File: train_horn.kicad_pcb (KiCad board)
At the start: 2 copper layers, 25.4 x 90 mm, 72 parts, among them J1 USB_OTG, J2 PROG, Q1 2N7002, SW1 PLAY, U1 MIC7221, U2 MCP73831, U3 TPS78233DDCR, U4 MSP430FR2000_TSSOP, U5 TPA6211A1

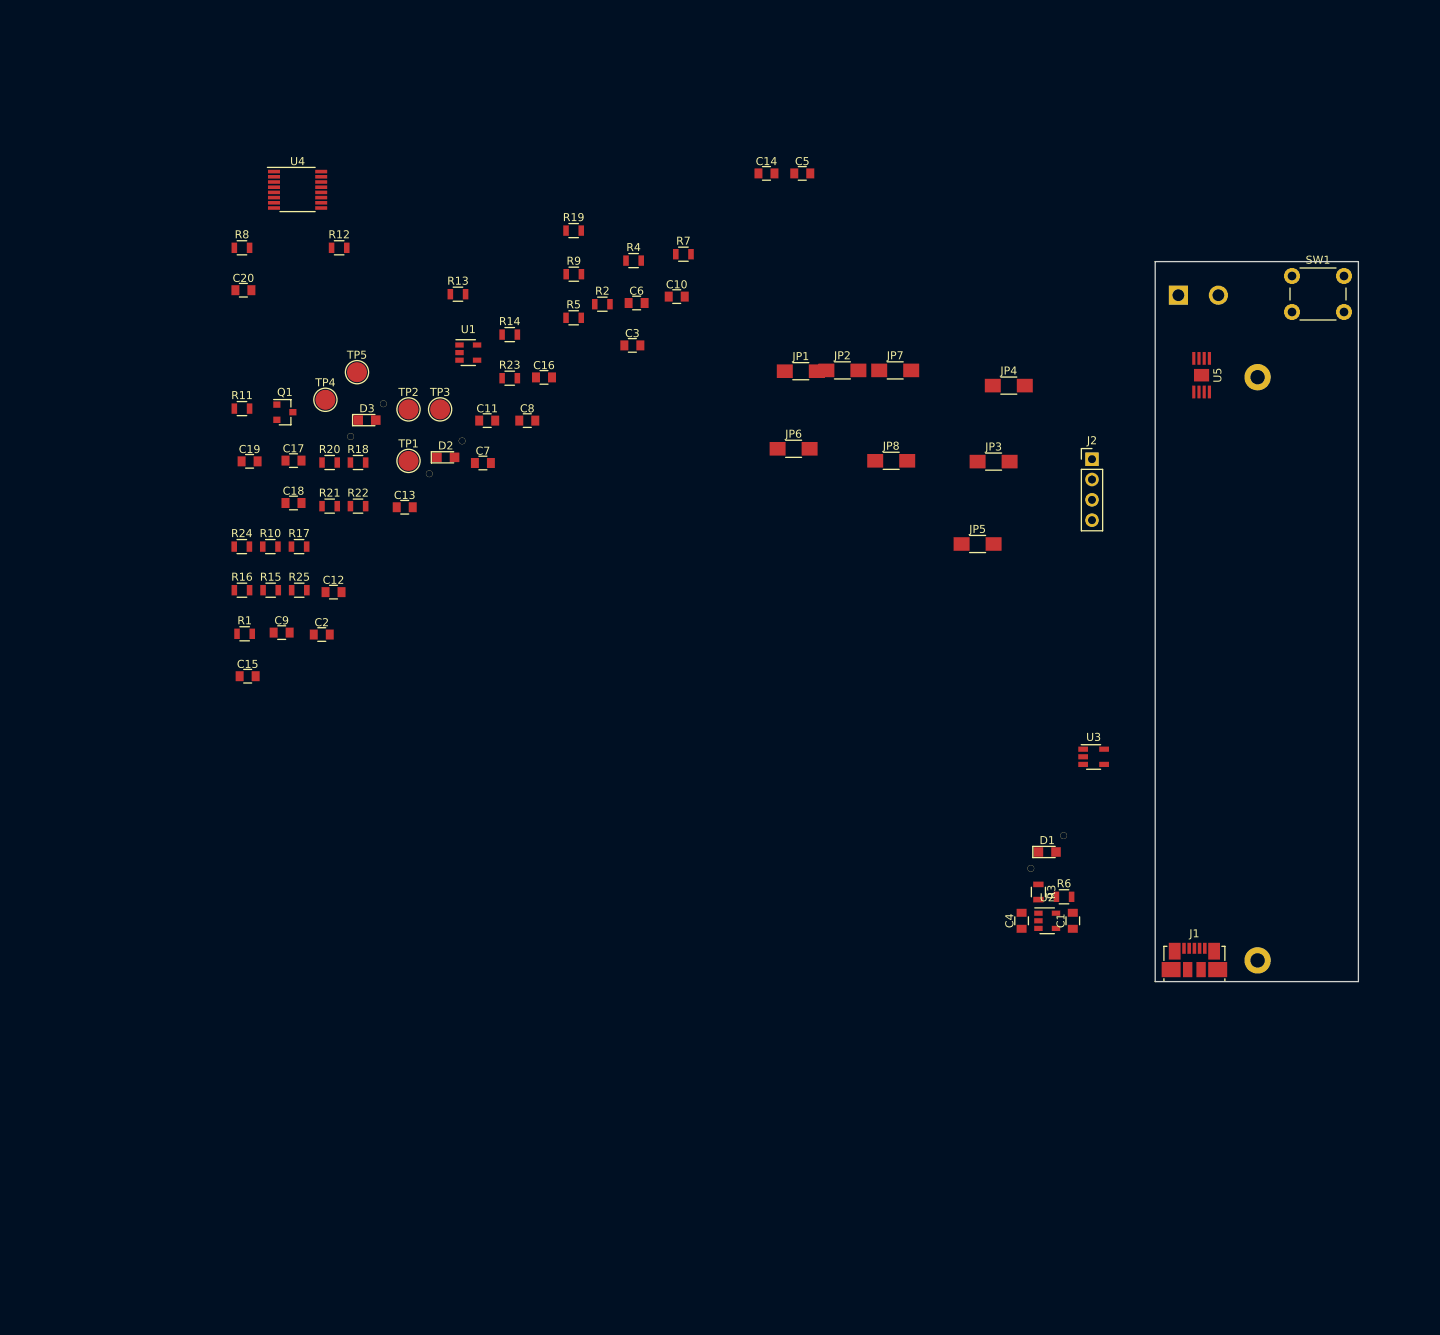
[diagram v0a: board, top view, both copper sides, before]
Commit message: setting large componet location. Change PCB size
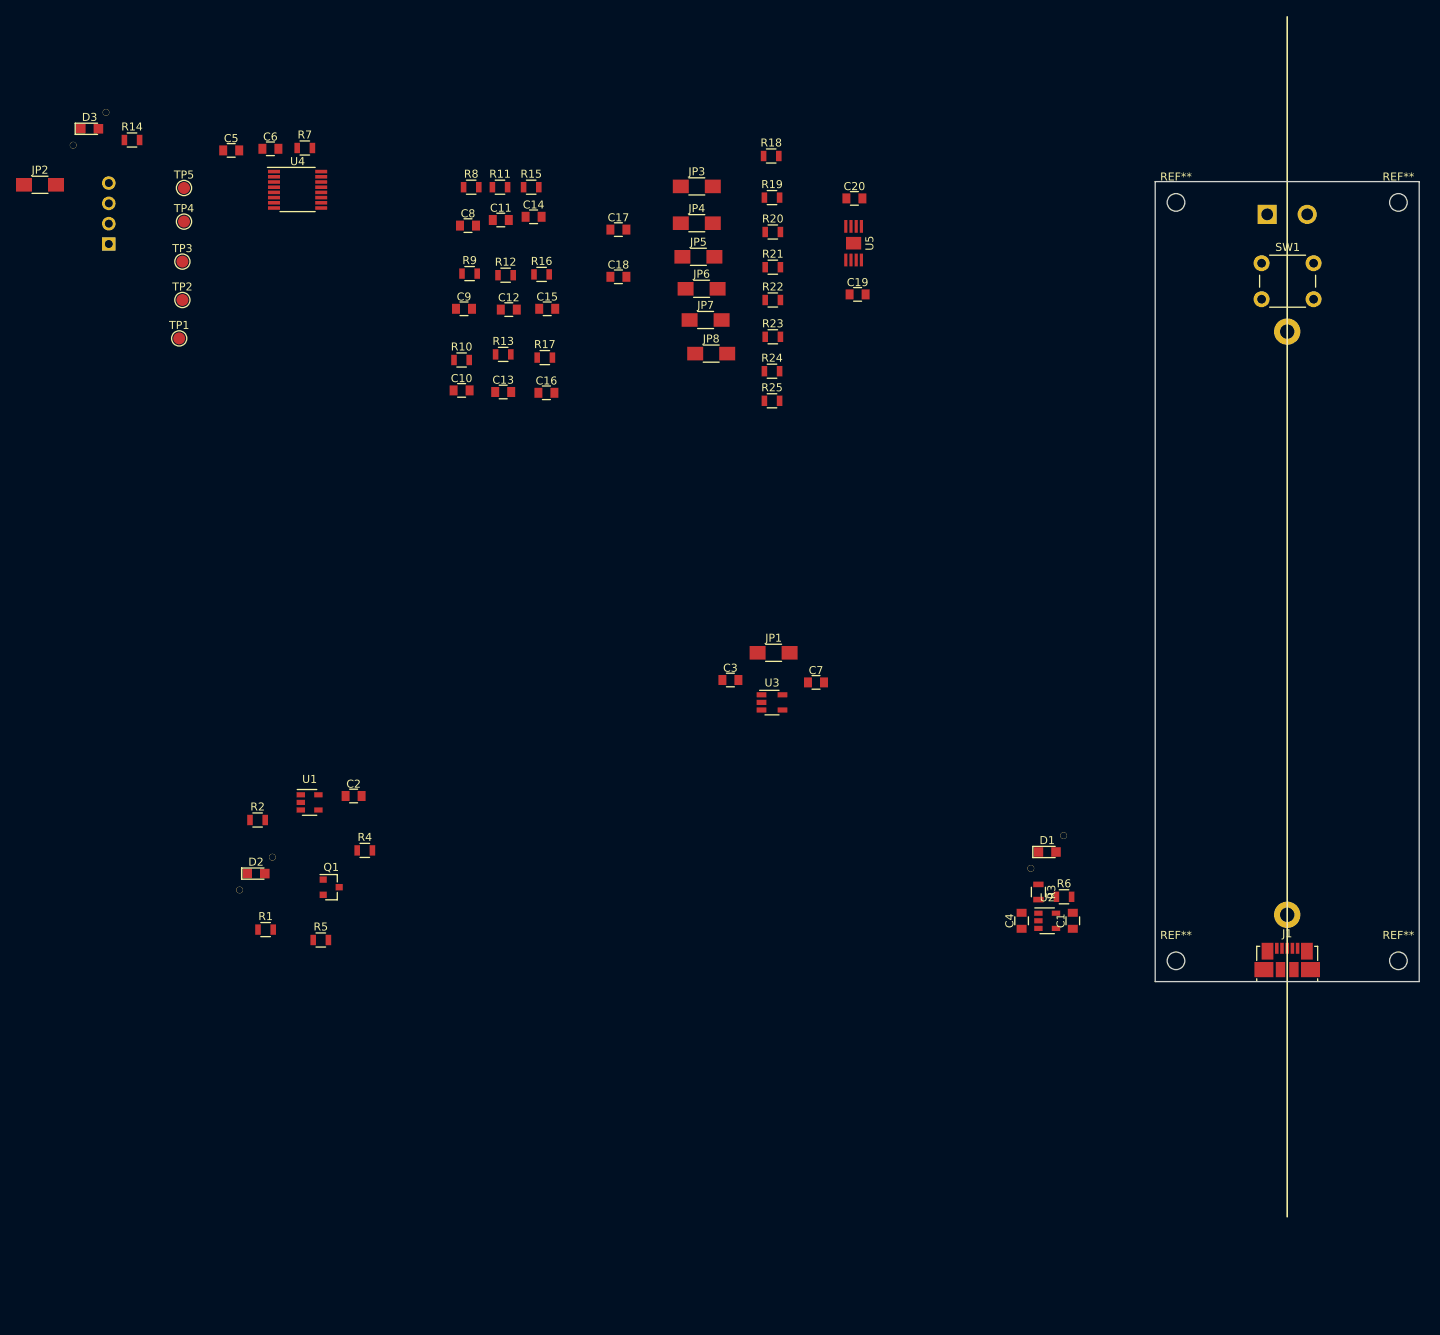
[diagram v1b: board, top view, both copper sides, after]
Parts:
- added REF**: MountingHole_2.2mm_M2, Mounting_Holes:MountingHole_2.2mm_M2, F.Cu at (241.6, 158.0)
- added REF**: MountingHole_2.2mm_M2, Mounting_Holes:MountingHole_2.2mm_M2, F.Cu at (213.8, 158.0)
- added REF**: MountingHole_2.2mm_M2, Mounting_Holes:MountingHole_2.2mm_M2, F.Cu at (213.8, 63.2)
- added REF**: MountingHole_2.2mm_M2, Mounting_Holes:MountingHole_2.2mm_M2, F.Cu at (241.6, 63.2)
- J2: moved to B.Cu
- TP1, TP2, TP3, TP4, TP5: footprint Connectors_TestPoints:Test_Point_Pad_d2.5mm -> Connectors_TestPoints:Test_Point_Pad_d1.5mm
- moved J2 125.8 mm to (80.4, 68.4)
- moved JP2 102.9 mm to (71.8, 61.0)
- moved R5 84.0 mm to (106.9, 155.4)
- moved R4 81.0 mm to (112.4, 144.2)
- moved C19 78.8 mm to (174.0, 74.7)
- moved R2 77.6 mm to (99.0, 140.4)
- moved C20 77.2 mm to (173.6, 62.7)
- moved C5 71.4 mm to (95.7, 56.7)
- moved R24 69.8 mm to (163.3, 84.3)
- moved R18 64.3 mm to (163.2, 57.4)
- moved R25 63.7 mm to (163.3, 88.0)
- moved R21 62.9 mm to (163.4, 71.3)
- moved R20 62.4 mm to (163.4, 66.9)
- moved R15 60.0 mm to (133.2, 61.3)
- moved Q1 59.7 mm to (108.2, 148.8)
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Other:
- board size 25.4 x 90 mm -> 33 x 100 mm

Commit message: moving things around
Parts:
- moved TP5 167.5 mm to (241.7, 132.1)
- moved TP4 164.8 mm to (241.7, 129.5)
- moved TP3 162.2 mm to (241.7, 126.9)
- moved TP2 159.8 mm to (241.7, 124.3)
- moved D3 159.3 mm to (214.3, 136.4), turned to 180 degrees
- moved TP1 158.0 mm to (241.7, 121.7)
- moved JP2 157.4 mm to (217.4, 120.9), turned to 90 degrees
- moved R14 152.2 mm to (221.4, 119.4)
- moved C5 143.7 mm to (222.4, 124.5), turned to 270 degrees
- moved J2 143.0 mm to (214.0, 119.5), turned to 180 degrees
- moved U4 138.2 mm to (227.7, 123.3)
- moved C6 137.8 mm to (220.4, 124.5), turned to 270 degrees
- moved R7 133.4 mm to (221.4, 121.4)
- moved R2 128.8 mm to (227.7, 145.4)
- moved R1 124.9 mm to (224.5, 143.9), turned to 270 degrees
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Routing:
- added copper zone on B.Cu, net GND

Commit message: laying things out
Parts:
- added REF**: VIA_06mm, lib_fp:VIA_0-4mm, F.Cu at (232.7, 71.7)
- added REF**: VIA_06mm, lib_fp:VIA_0-6mm, F.Cu at (236.4, 144.8)
- added REF**: VIA_06mm, lib_fp:VIA_0-6mm, F.Cu at (235.4, 143.8)
- added REF**: VIA_06mm, lib_fp:VIA_0-6mm, F.Cu at (226.3, 149.7)
- added REF**: VIA_06mm, lib_fp:VIA_0-6mm, F.Cu at (227.7, 149.7)
- added REF**: VIA_06mm, lib_fp:VIA_0-6mm, F.Cu at (229.0, 149.7)
- added REF**: VIA_06mm, lib_fp:VIA_0-6mm, F.Cu at (226.3, 148.7)
- added REF**: VIA_06mm, lib_fp:VIA_0-6mm, F.Cu at (227.7, 148.7)
- added REF**: VIA_06mm, lib_fp:VIA_0-6mm, F.Cu at (232.9, 149.7)
- added REF**: VIA_06mm, lib_fp:VIA_0-6mm, F.Cu at (234.2, 149.7)
- added REF**: VIA_06mm, lib_fp:VIA_0-6mm, F.Cu at (235.6, 149.7)
- added REF**: VIA_06mm, lib_fp:VIA_0-4mm, F.Cu at (231.9, 71.7)
- added REF**: VIA_06mm, lib_fp:VIA_0-6mm, F.Cu at (232.9, 148.7)
- added REF**: VIA_06mm, lib_fp:VIA_0-6mm, F.Cu at (234.2, 148.7)
- added REF**: VIA_06mm, lib_fp:VIA_0-6mm, F.Cu at (235.6, 148.7)
- added REF**: VIA_06mm, lib_fp:VIA_0-6mm, F.Cu at (229.0, 148.7)
- added REF**: VIA_06mm, lib_fp:VIA_0-6mm, F.Cu at (236.4, 143.8)
- added REF**: VIA_06mm, lib_fp:VIA_0-6mm, F.Cu at (225.4, 144.3)
- added REF**: VIA_06mm, lib_fp:VIA_0-4mm, F.Cu at (232.7, 70.5)
- added REF**: VIA_06mm, lib_fp:VIA_0-4mm, F.Cu at (232.3, 71.1)
- added REF**: VIA_06mm, lib_fp:VIA_0-4mm, F.Cu at (231.9, 70.5)
- added REF**: VIA_06mm, lib_fp:VIA_0-6mm, F.Cu at (226.6, 145.6)
- added REF**: VIA_06mm, lib_fp:VIA_0-6mm, F.Cu at (225.4, 145.6)
- added REF**: VIA_06mm, lib_fp:VIA_0-6mm, F.Cu at (226.6, 144.3)
- added REF**: VIA_06mm, lib_fp:VIA_0-6mm, F.Cu at (235.4, 145.8)
- added REF**: VIA_06mm, lib_fp:VIA_0-6mm, F.Cu at (236.4, 145.8)
- added REF**: VIA_06mm, lib_fp:VIA_0-6mm, F.Cu at (235.4, 144.8)
- BT1: footprint lib_fp:18650_battery_holder_PCB_Pins -> 18650_battery_holder_PCB_Pins
- D1: footprint lib_fp:LED_0805_LIGHTPIPE -> LED_0805_LIGHTPIPE
- J1: footprint Connectors_USB:USB_Micro-B_Molex_47346-0001 -> USB_Micro-B_Amphenol_10118192-0001LF
- JP2: footprint Resistors_SMD:R_1206_HandSoldering -> Pin_Headers:Pin_Header_Straight_1x02_Pitch2.54mm; moved to B.Cu
- SW1: footprint Buttons_Switches_THT:SW_PUSH_6mm -> SWITCH_Panasonic_SMDRight_EVQP7C
- U5: footprint lib_fp:TPA6211A1_MSOP -> TPA6211A1_MSOP
- moved C4 67.5 mm to (227.8, 146.7), turned to 90 degrees
- moved J1 67.3 mm to (242.8, 147.8)
- moved U2 64.1 mm to (230.9, 146.7), turned to 0 degrees
- moved R3 62.0 mm to (229.8, 143.1), turned to 270 degrees
- moved C1 60.9 mm to (234.2, 146.7), turned to 90 degrees
- moved R6 59.1 mm to (233.1, 143.7), turned to 0 degrees
- moved D1 54.5 mm to (241.2, 139.1), turned to 0 degrees
- moved D2 28.5 mm to (241.2, 133.1), turned to 0 degrees
- moved D3 28.5 mm to (241.2, 127.1), turned to 0 degrees
- moved R22 26.6 mm to (240.1, 79.3), turned to 180 degrees
- moved C18 26.0 mm to (236.5, 79.3), turned to 180 degrees
- moved C19 23.6 mm to (237.2, 72.0), turned to 0 degrees
- moved R23 23.1 mm to (240.1, 81.8), turned to 180 degrees
- moved R24 19.7 mm to (240.1, 84.3), turned to 180 degrees
- moved JP8 19.5 mm to (235.1, 81.8), turned to 0 degrees
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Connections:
- JP3 pad 2: Net-(JP3-Pad2) -> Net-(C17-Pad2)
- JP4 pad 1: Net-(JP3-Pad2) -> Net-(JP4-Pad1)
- JP4 pad 2: Net-(JP4-Pad2) -> Net-(JP3-Pad1)
- JP5 pad 1: Net-(JP4-Pad2) -> Net-(JP5-Pad1)
- JP5 pad 2: Net-(C17-Pad2) -> Net-(JP4-Pad1)
- JP6 pad 1: Net-(C18-Pad1) -> Net-(JP6-Pad1)
- JP7 pad 1: Net-(JP6-Pad2) -> Net-(JP7-Pad1)
- JP7 pad 2: Net-(JP7-Pad2) -> Net-(JP6-Pad1)
- JP8 pad 1: Net-(JP7-Pad2) -> Net-(C18-Pad1)
- JP8 pad 2: Net-(JP8-Pad2) -> Net-(JP7-Pad1)
- R18 pad 2: Net-(JP3-Pad1) -> Net-(JP5-Pad1)
- R19 pad 2: Net-(JP3-Pad2) -> Net-(JP4-Pad1)
- R20 pad 2: Net-(JP4-Pad2) -> Net-(JP3-Pad1)
- R23 pad 2: Net-(JP6-Pad2) -> Net-(JP7-Pad1)
- R24 pad 2: Net-(JP7-Pad2) -> Net-(JP6-Pad1)
- R25 pad 2: Net-(JP8-Pad2) -> Net-(JP6-Pad2)
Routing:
- net VCC: track 0.00 -> 83.2 mm
- net GND: track 0.00 -> 33.3 mm, vias 0 -> 26
- net Net-(Q1-Pad1): track 0.00 -> 28.9 mm
- net Net-(R18-Pad1): track 0.00 -> 26.7 mm
- net Net-(C1-Pad1): track 0.07 -> 20.2 mm
- net +3V3: track 0.00 -> 16.7 mm
- net PLAY_LED: track 0.00 -> 16.4 mm
- net Net-(C14-Pad1): track 0.00 -> 15.6 mm
- net Net-(R22-Pad1): track 0.00 -> 14.8 mm
- net Net-(D1-Pad1): track 0.00 -> 13.6 mm
- net SBWTDIO: track 0.00 -> 12.8 mm
- net Net-(LS1-Pad1): track 0.00 -> 12.4 mm
- net SBWTCK: track 0.00 -> 12.1 mm
- net Net-(C17-Pad2): track 0.00 -> 7.55 mm
- net Net-(C18-Pad1): track 0.00 -> 7.55 mm
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- added copper zone on F.Cu, net GND
- added copper zone on B.Cu, net Net-(C1-Pad1)
- added copper zone on F.Cu, net Net-(C1-Pad1)
- added copper zone on F.Cu, net Net-(J1-Pad6)
- added copper zone on F.Cu, net Net-(R18-Pad1)
- added copper zone on F.Cu, net Net-(R22-Pad1)
- added copper zone on B.Cu, net VCC
- added copper zone on F.Cu, net VCC
- removed copper zone on B.Cu, net GND
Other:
- net class Power added: clearance 0.2, trace_width 1.25, via_dia 2.5, via_drill 1.25

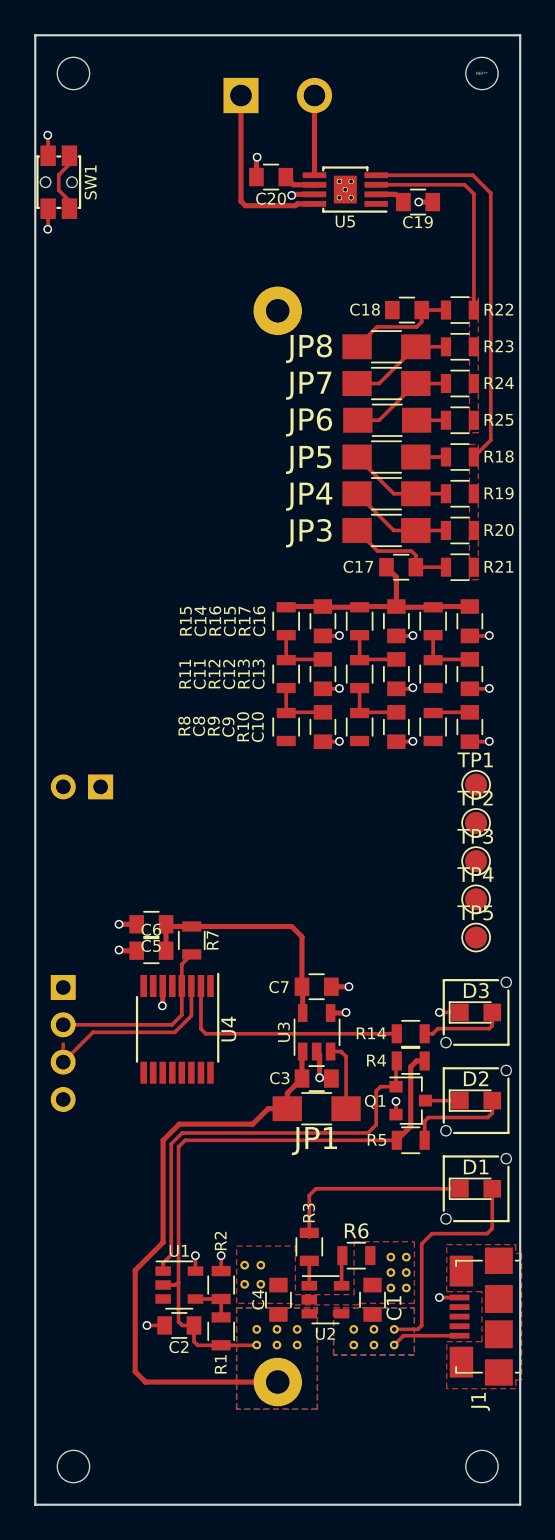
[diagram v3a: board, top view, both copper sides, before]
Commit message: finising touches on silkscreen
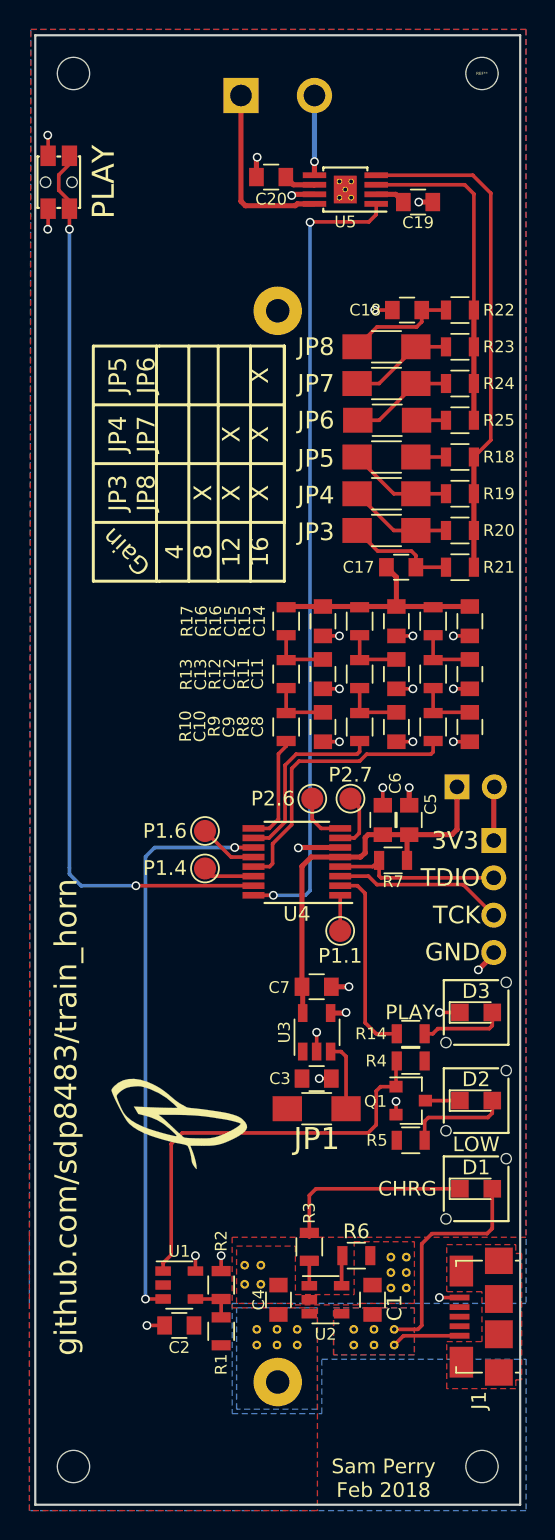
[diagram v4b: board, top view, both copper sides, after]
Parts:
- added G***: LOGO, lib_fp:logo_9x6mm, F.Cu at (221.0, 134.7)
- TP1: value P1.3 -> P1.1
- moved J2 31.0 mm to (242.4, 115.4)
- moved JP2 24.2 mm to (239.9, 111.8), turned to 270 degrees
- moved C5 18.9 mm to (236.7, 114.0), turned to 90 degrees
- moved TP2 18.7 mm to (222.8, 117.3)
- moved TP3 18.6 mm to (222.8, 114.8)
- moved C6 18.1 mm to (234.8, 114.0), turned to 90 degrees
- moved R7 14.7 mm to (235.6, 116.8), turned to 180 degrees
- moved U4 14.0 mm to (229.0, 116.8), turned to 180 degrees
- moved TP1 13.6 mm to (231.9, 121.5)
- moved TP4 13.1 mm to (230.1, 112.5)
- moved TP5 12.7 mm to (232.7, 112.5)
- moved C10 10.0 mm to (230.8, 107.7)
- moved C11 10.0 mm to (240.8, 104.1)
- moved C13 10.0 mm to (230.8, 104.1)
- moved C14 10.0 mm to (240.8, 100.5)
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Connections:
- REF** pad 1: (no net) -> GND (x10)
- U4 pad 1: PLAY -> Net-(TP1-Pad1)
- U4 pad 15: Net-(TP1-Pad1) -> PLAY
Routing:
- net VCC: track 83.2 -> 2.37 mm
- net PLAY: track 4.20 -> 62.4 mm, vias 0 -> 2
- net ~SHDWN: track 0.00 -> 54.9 mm, vias 0 -> 2
- net VREF+: track 0.00 -> 38.9 mm, vias 0 -> 2
- net B3: track 0.00 -> 19.2 mm
- net D#4: track 0.00 -> 12.6 mm
- net +3V3: track 16.7 -> 27.0 mm
- net A4: track 0.00 -> 8.03 mm
- net Net-(R22-Pad1): track 14.8 -> 22.3 mm
- net Net-(R18-Pad1): track 26.7 -> 34.2 mm
- net Net-(TP3-Pad1): track 0.00 -> 4.04 mm
- net Net-(TP5-Pad1): track 0.00 -> 4.03 mm
- net Net-(J2-Pad1): track 0.00 -> 3.67 mm
- net Net-(TP4-Pad1): track 0.00 -> 3.57 mm
- net Net-(TP2-Pad1): track 0.00 -> 3.52 mm
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- added copper zone on B.Cu, net GND
- removed copper zone on F.Cu, net Net-(R18-Pad1)
- removed copper zone on F.Cu, net Net-(R22-Pad1)
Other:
- board text added: "+"
- board text added: "-"
- board text added: "18650 LiPo Cell Only"
- board text added: "3V3"
- board text added: "4 8 12 16"
- board text added: "8-4Ω SPEAKER"
- board text added: "CHRG"
- board text added: "EXT 3V3"
- board text added: "GND"
- board text added: "Gain"
- board text added: "JP3 JP8 X X X"
- board text added: "JP4 JP7 X X"
- board text added: "JP5 JP6 X"
- board text added: "LOW"
- board text added: "P1.1"
- board text added: "P1.4"
- board text added: "P1.6"
- board text added: "P2.6"
- board text added: "P2.7"
- board text added: "PLAY"
- board text added: "PROG"
- board text added: "Sam Perry Feb 2018"
- board text added: "TCK"
- board text added: "TDIO"
- board text added: "github.com/sdp8483/train_horn"
